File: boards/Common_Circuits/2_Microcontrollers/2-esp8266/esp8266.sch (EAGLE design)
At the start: 11 parts, among them X1 ESP-12

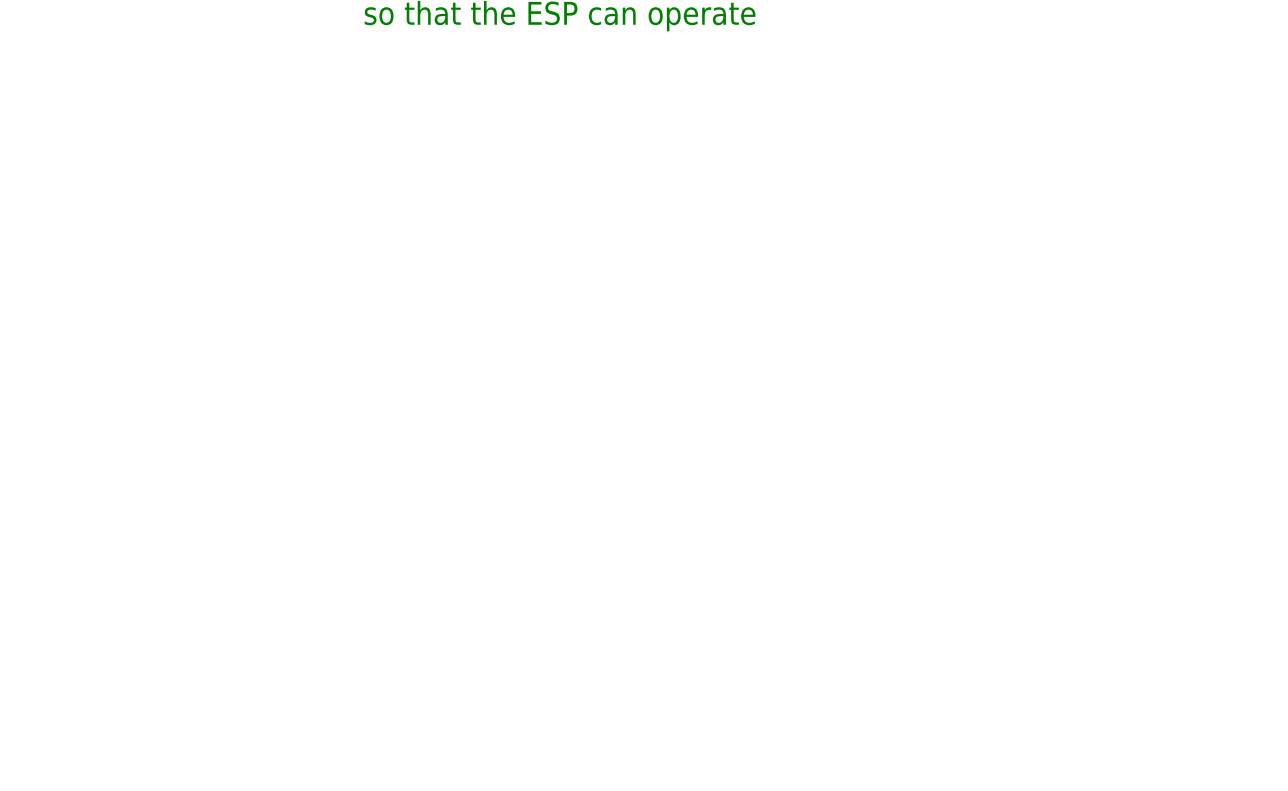
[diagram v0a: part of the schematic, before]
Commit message: adds ESP8266 board to common circuits
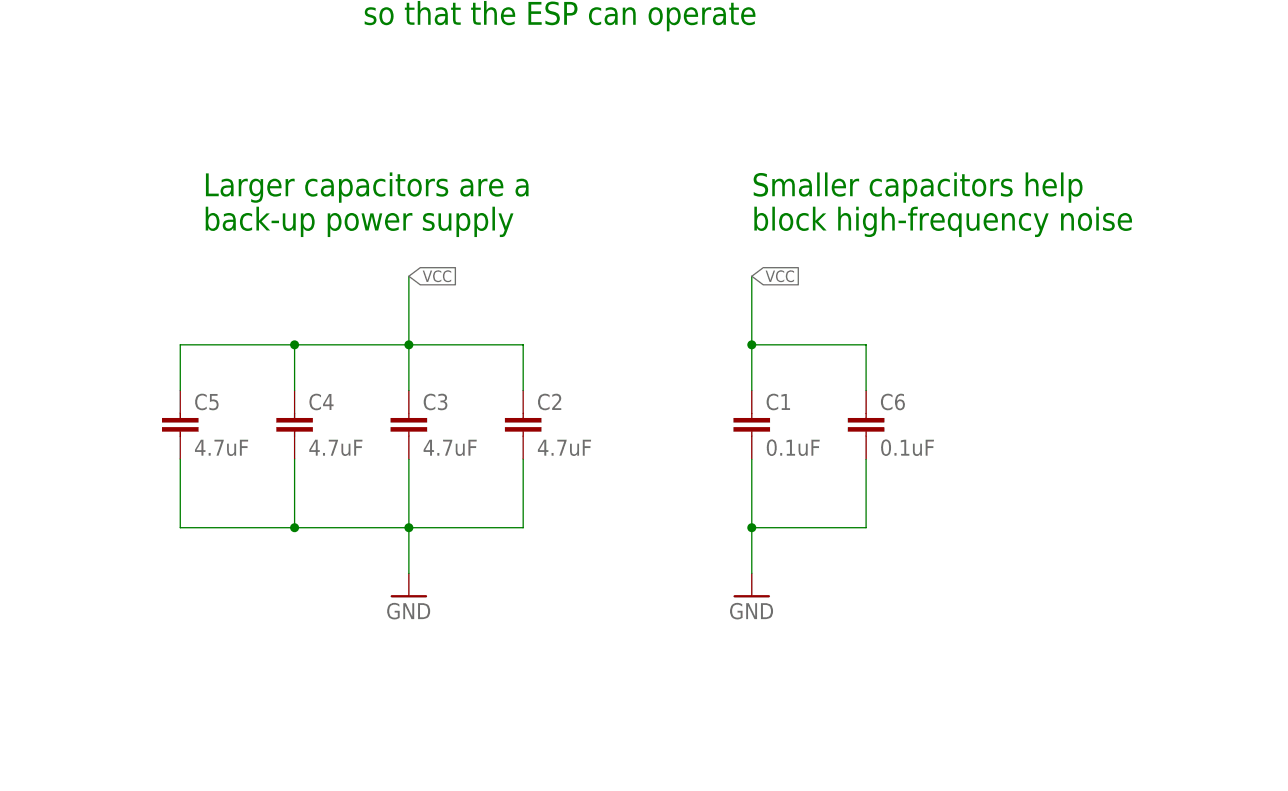
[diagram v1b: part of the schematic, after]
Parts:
- added C1, C6: 0.1uF, SparkFun-Capacitors:0.1UF-0603-25V-5%
- added C2, C3, C4, C5: 4.7uF, SparkFun-Capacitors:4.7UF0603
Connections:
- net GND: now also C1.2, C2.2, C3.2, C4.2, C5.2, C6.2
- net VCC: now also C1.1, C2.1, C3.1, C4.1, C5.1, C6.1
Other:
- note added: "Larger capacitors are a back-up power supply"
- note added: "Smaller capacitors help block high-frequency noise"
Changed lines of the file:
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@@
 <part name="P+2" library="supply1" library_urn="urn:adsk.eagle:library:371" deviceset="VCC" device=""/>
 <part name="GND1" library="supply1" deviceset="GND" device=""/>
+<part name="C1" library="SparkFun-Capacitors" deviceset="0.1UF" device="-0603-25V-5%" value="0.1uF"/>
+<part name="C2" library="SparkFun-Capacitors" deviceset="4.7UF" device="0603" value="4.7uF"/>
+<part name="C3" library="SparkFun-Capacitors" deviceset="4.7UF" device="0603" value="4.7uF"/>
+<part name="GND4" library="supply1" library_urn="urn:adsk.eagle:library:371" deviceset="GND" device=""/>
+<part name="GND5" library="supply1" library_urn="urn:adsk.eagle:library:371" deviceset="GND" device=""/>
+<part name="C4" library="SparkFun-Capacitors" deviceset="4.7UF" device="0603" value="4.7uF"/>
+<part name="C5" library="SparkFun-Capacitors" deviceset="4.7UF" device="0603" value="4.7uF"/>
+<part name="C6" library="SparkFun-Capacitors" deviceset="0.1UF" device="-0603-25V-5%" value="0.1uF"/>
 </parts>
 <sheets>
@@
 Read more about it on Adafruit:
 https://learn.adafruit.com/adafruit-huzzah-esp8266-breakout/using-arduino-ide#blink-test</text>
+<text x="154.94" y="78.74" size="2.54" layer="91">Smaller capacitors help
+block high-frequency noise</text>
+<text x="93.98" y="78.74" size="2.54" layer="91">Larger capacitors are a
+back-up power supply</text>
 </plain>
 <instances>
@@
 <instance part="P+2" gate="VCC" x="50.8" y="53.34" rot="R270"/>
 <instance part="GND1" gate="1" x="38.1" y="45.72"/>
+<instance part="C1" gate="G$1" x="154.94" y="55.88"/>
+<instance part="C2" gate="G$1" x="129.54" y="55.88"/>
+<instance part="C3" gate="G$1" x="116.84" y="55.88"/>
+<instance part="GND4" gate="1" x="116.84" y="38.1"/>
+<instance part="GND5" gate="1" x="154.94" y="38.1"/>
+<instance part="C4" gate="G$1" x="104.14" y="55.88"/>
+<instance part="C5" gate="G$1" x="91.44" y="55.88"/>
+<instance part="C6" gate="G$1" x="167.64" y="55.88"/>
 </instances>
 <busses>
@@
 <wire x1="38.1" y1="50.8" x2="38.1" y2="48.26" width="0.1524" layer="91"/>
 <pinref part="GND1" gate="1" pin="GND"/>
+</segment>
+<segment>
+<pinref part="C3" gate="G$1" pin="2"/>
+<wire x1="116.84" y1="53.34" x2="116.84" y2="45.72" width="0.1524" layer="91"/>
+<pinref part="C2" gate="G$1" pin="2"/>
+<wire x1="116.84" y1="45.72" x2="129.54" y2="45.72" width="0.1524" layer="91"/>
+<wire x1="129.54" y1="45.72" x2="129.54" y2="53.34" width="0.1524" layer="91"/>
+<pinref part="GND4" gate="1" pin="GND"/>
+<wire x1="116.84" y1="45.72" x2="116.84" y2="40.64" width="0.1524" layer="91"/>
+<junction x="116.84" y="45.72"/>
+<pinref part="C4" gate="G$1" pin="2"/>
+<wire x1="116.84" y1="45.72" x2="104.14" y2="45.72" width="0.1524" layer="91"/>
+<wire x1="104.14" y1="45.72" x2="104.14" y2="53.34" width="0.1524" layer="91"/>
+<pinref part="C5" gate="G$1" pin="2"/>
+<wire x1="104.14" y1="45.72" x2="91.44" y2="45.72" width="0.1524" layer="91"/>
+<wire x1="91.44" y1="45.72" x2="91.44" y2="53.34" width="0.1524" layer="91"/>
+<junction x="104.14" y="45.72"/>
+</segment>
+<segment>
+<pinref part="C1" gate="G$1" pin="2"/>
+<wire x1="154.94" y1="53.34" x2="154.94" y2="45.72" width="0.1524" layer="91"/>
+<pinref part="GND5" gate="1" pin="GND"/>
+<pinref part="C6" gate="G$1" pin="2"/>
+<wire x1="154.94" y1="45.72" x2="154.94" y2="40.64" width="0.1524" layer="91"/>
+<wire x1="154.94" y1="45.72" x2="167.64" y2="45.72" width="0.1524" layer="91"/>
+<wire x1="167.64" y1="45.72" x2="167.64" y2="53.34" width="0.1524" layer="91"/>
+<junction x="154.94" y="45.72"/>
 </segment>
 </net>
@@
 <pinref part="P+2" gate="VCC" pin="VCC"/>
 </segment>
-</net>
+<segment>
+<pinref part="C3" gate="G$1" pin="1"/>
+<wire x1="116.84" y1="60.96" x2="116.84" y2="66.04" width="0.1524" layer="91"/>
+<pinref part="C2" gate="G$1" pin="1"/>
+<wire x1="116.84" y1="66.04" x2="129.54" y2="66.04" width="0.1524" layer="91"/>
+<wire x1="129.54" y1="66.04" x2="129.54" y2="60.96" width="0.1524" layer="91"/>
+<wire x1="116.84" y1="66.04" x2="116.84" y2="73.66" width="0.1524" layer="91"/>
+<junction x="116.84" y="66.04"/>
+<label x="116.84" y="73.66" size="1.27" layer="95" xref="yes"/>
+<pinref part="C4" gate="G$1" pin="1"/>
+<wire x1="116.84" y1="66.04" x2="104.14" y2="66.04" width="0.1524" layer="91"/>
+<wire x1="104.14" y1="66.04" x2="104.14" y2="60.96" width="0.1524" layer="91"/>
+<pinref part="C5" gate="G$1" pin="1"/>
+<wire x1="104.14" y1="66.04" x2="91.44" y2="66.04" width="0.1524" layer="91"/>
+<wire x1="91.44" y1="66.04" x2="91.44" y2="60.96" width="0.1524" layer="91"/>
+<junction x="104.14" y="66.04"/>
+</segment>
+<segment>
+<pinref part="C1" gate="G$1" pin="1"/>
+<wire x1="154.94" y1="60.96" x2="154.94" y2="66.04" width="0.1524" layer="91"/>
+<label x="154.94" y="73.66" size="1.27" layer="95" xref="yes"/>
+<pinref part="C6" gate="G$1" pin="1"/>
+<wire x1="154.94" y1="66.04" x2="154.94" y2="73.66" width="0.1524" layer="91"/>
+<wire x1="154.94" y1="66.04" x2="167.64" y2="66.04" width="0.1524" layer="91"/>
+<wire x1="167.64" y1="66.04" x2="167.64" y2="60.96" width="0.1524" layer="91"/>
+<junction x="154.94" y="66.04"/>
+</segment>
+</net>

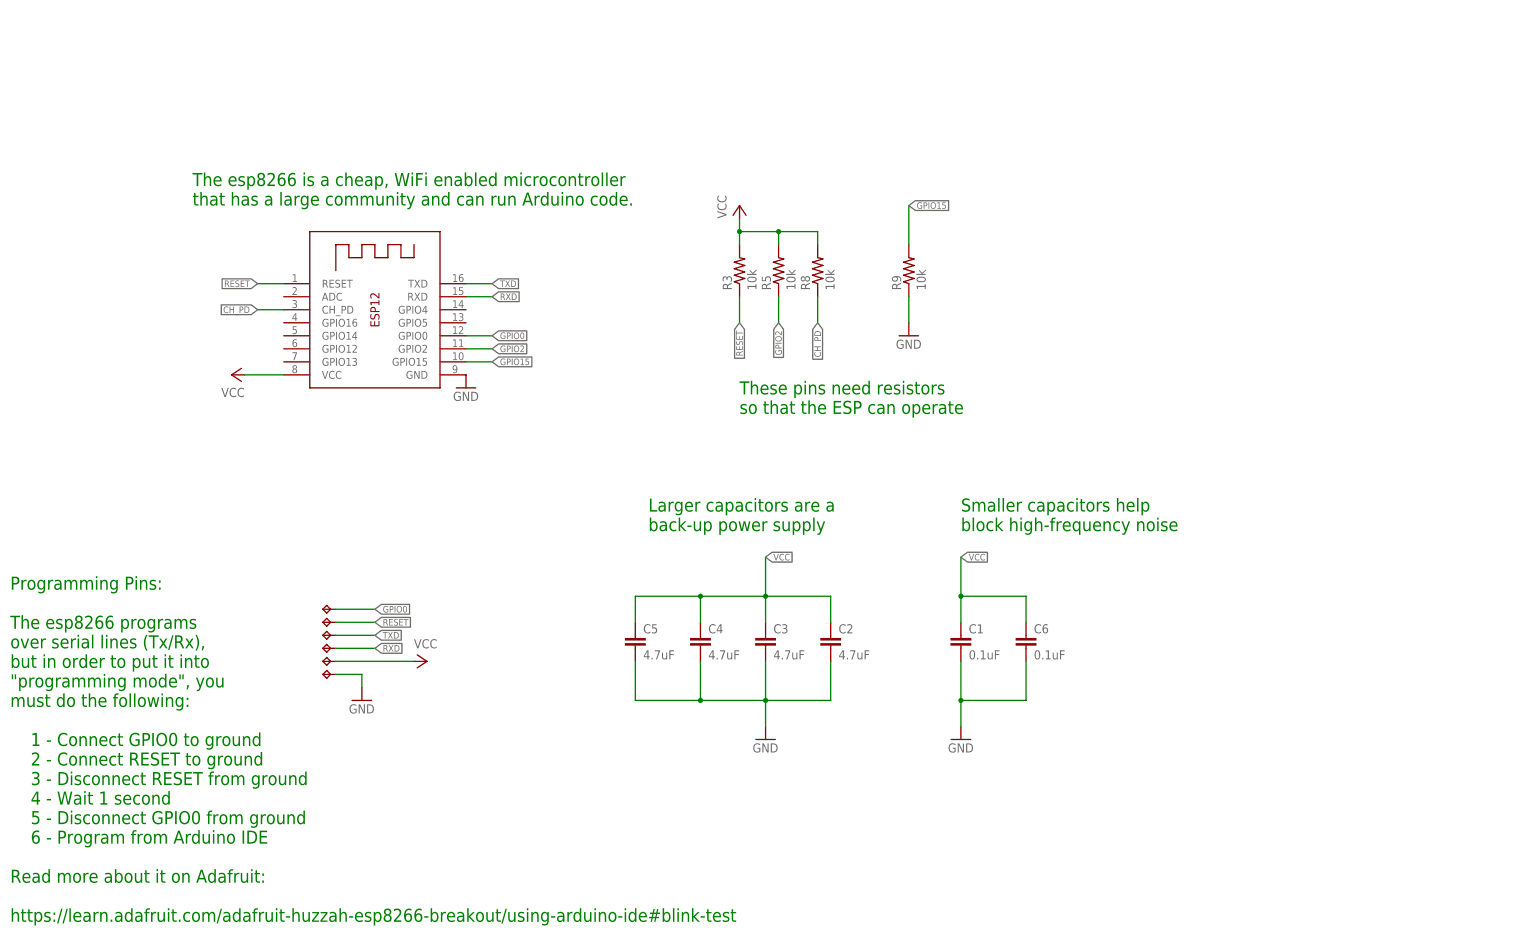
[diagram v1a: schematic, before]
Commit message: adds REgulators example to common circuits
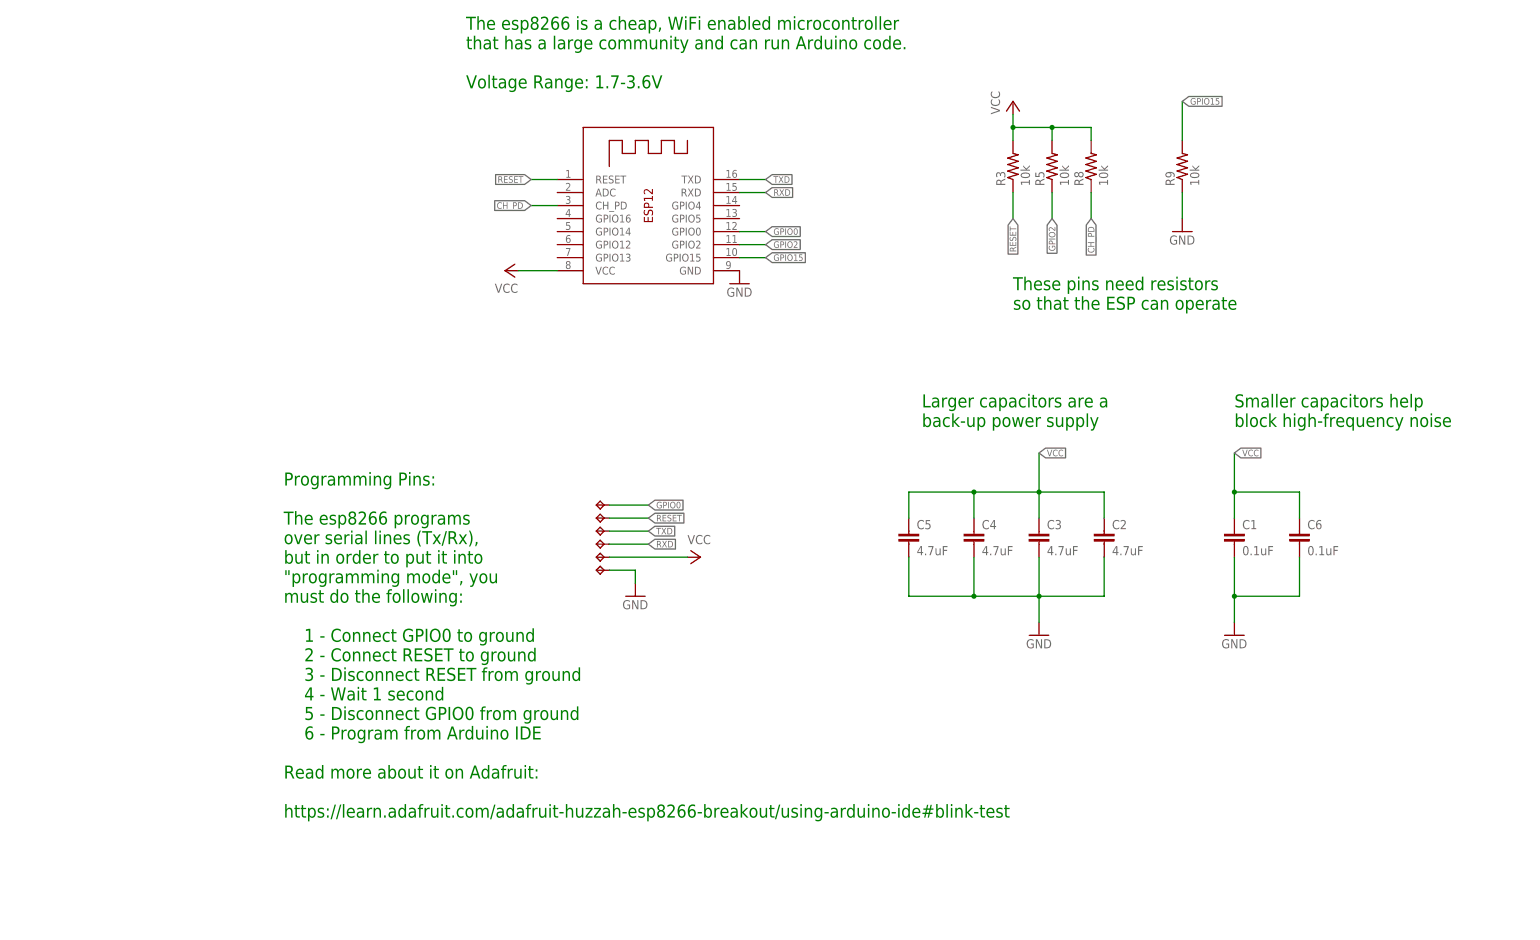
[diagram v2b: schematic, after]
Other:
- note added: "The esp8266 is a cheap, WiFi enabled microcontroller that has a large community and can run Arduino code. Voltage Range: 1.7-3.6V"
- note removed: "The esp8266 is a cheap, WiFi enabled microcontroller that has a large community and can run Arduino code."
- moved on the sheet: C1, C2, C3, C4, C5, C6, R3, R5, R8, R9
